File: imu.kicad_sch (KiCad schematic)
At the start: 4 parts, among them U8 MC3479

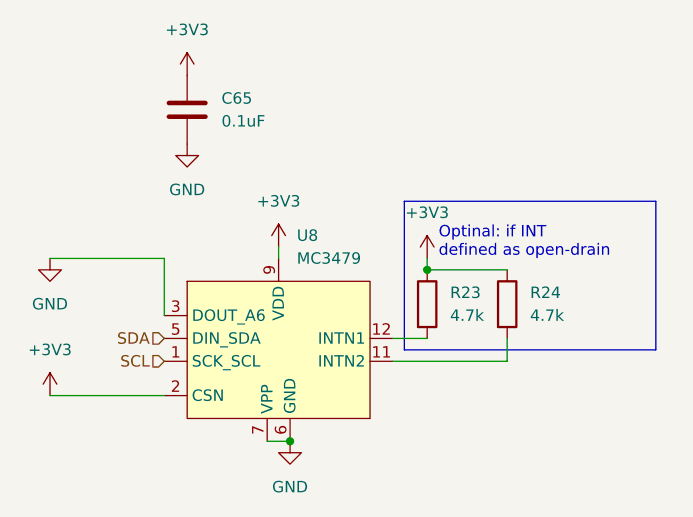
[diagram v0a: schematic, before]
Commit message: done first iteration of pcb routing, slikscreen still broken
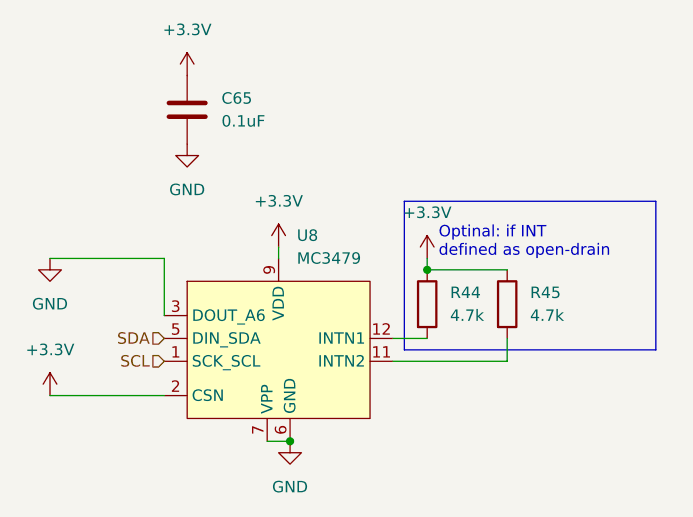
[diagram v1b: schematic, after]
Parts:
- renumbered R23 to R44, R24 to R45
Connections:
- net +3V3 renamed +3.3V
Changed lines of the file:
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@@
     (pin "2")
   )
-  (symbol (lib_id "power:+3V3") (at 140.97 86.36 0) (unit 1)
+  (symbol (lib_id "power:+3.3V") (at 140.97 86.36 0) (unit 1)
     (in_bom yes) (on_board yes) (fields_autoplaced)
-    (property "Reference" "#PWR075" (id 0) (at 140.97 90.17 0)
+    (property "Reference" "#PWR0235" (id 0) (at 140.97 90.17 0)
       (effects (font (size 1.27 1.27)) hide)
     )
-    (property "Value" "+3V3" (id 1) (at 140.97 81.28 0))
+    (property "Value" "+3.3V" (id 1) (at 140.97 81.28 0))
     (property "Footprint" "" (id 2) (at 140.97 86.36 0)
       (effects (font (size 1.27 1.27)) hide)
@@
   (symbol (lib_id "Device:R") (at 157.48 92.71 0) (unit 1)
     (in_bom yes) (on_board yes) (fields_autoplaced)
-    (property "Reference" "R23" (id 0) (at 160.02 91.4399 0)
+    (property "Reference" "R44" (id 0) (at 160.02 91.4399 0)
       (effects (font (size 1.27 1.27)) (justify left))
     )
@@
     (pin "2")
   )
-  (symbol (lib_id "power:+3V3") (at 130.81 67.31 0) (unit 1)
+  (symbol (lib_id "power:+3.3V") (at 130.81 67.31 0) (unit 1)
     (in_bom yes) (on_board yes) (fields_autoplaced)
-    (property "Reference" "#PWR073" (id 0) (at 130.81 71.12 0)
+    (property "Reference" "#PWR0234" (id 0) (at 130.81 71.12 0)
       (effects (font (size 1.27 1.27)) hide)
     )
-    (property "Value" "+3V3" (id 1) (at 130.81 62.23 0))
+    (property "Value" "+3.3V" (id 1) (at 130.81 62.23 0))
     (property "Footprint" "" (id 2) (at 130.81 67.31 0)
       (effects (font (size 1.27 1.27)) hide)
@@
     (pin "1")
   )
-  (symbol (lib_id "power:+3V3") (at 115.57 102.87 0) (unit 1)
-    (in_bom yes) (on_board yes) (fields_autoplaced)
-    (property "Reference" "#PWR072" (id 0) (at 115.57 106.68 0)
-      (effects (font (size 1.27 1.27)) hide)
-    )
-    (property "Value" "+3V3" (id 1) (at 115.57 97.79 0))
-    (property "Footprint" "" (id 2) (at 115.57 102.87 0)
-      (effects (font (size 1.27 1.27)) hide)
-    )
-    (property "Datasheet" "" (id 3) (at 115.57 102.87 0)
-      (effects (font (size 1.27 1.27)) hide)
-    )
-    (pin "1")
-  )
   (symbol (lib_id "power:GND") (at 115.57 87.63 0) (unit 1)
     (in_bom yes) (on_board yes) (fields_autoplaced)
-    (property "Reference" "#PWR071" (id 0) (at 115.57 93.98 0)
+    (property "Reference" "#PWR074" (id 0) (at 115.57 93.98 0)
       (effects (font (size 1.27 1.27)) hide)
     )
@@
   (symbol (lib_id "Device:R") (at 166.37 92.71 0) (unit 1)
     (in_bom yes) (on_board yes) (fields_autoplaced)
-    (property "Reference" "R24" (id 0) (at 168.91 91.4399 0)
+    (property "Reference" "R45" (id 0) (at 168.91 91.4399 0)
       (effects (font (size 1.27 1.27)) (justify left))
     )
@@
     (pin "2")
   )
-  (symbol (lib_id "power:+3V3") (at 157.48 87.63 0) (unit 1)
+  (symbol (lib_id "power:+3.3V") (at 157.48 87.63 0) (unit 1)
     (in_bom yes) (on_board yes) (fields_autoplaced)
-    (property "Reference" "#PWR077" (id 0) (at 157.48 91.44 0)
+    (property "Reference" "#PWR0233" (id 0) (at 157.48 91.44 0)
       (effects (font (size 1.27 1.27)) hide)
     )
-    (property "Value" "+3V3" (id 1) (at 157.48 82.55 0))
+    (property "Value" "+3.3V" (id 1) (at 157.48 82.55 0))
     (property "Footprint" "" (id 2) (at 157.48 87.63 0)
       (effects (font (size 1.27 1.27)) hide)
@@
   (symbol (lib_id "power:GND") (at 142.24 107.95 0) (unit 1)
     (in_bom yes) (on_board yes) (fields_autoplaced)
-    (property "Reference" "#PWR076" (id 0) (at 142.24 114.3 0)
+    (property "Reference" "#PWR079" (id 0) (at 142.24 114.3 0)
       (effects (font (size 1.27 1.27)) hide)
     )
@@
     (pin "1")
   )
+  (symbol (lib_id "power:+3.3V") (at 115.57 102.87 0) (unit 1)
+    (in_bom yes) (on_board yes) (fields_autoplaced)
+    (property "Reference" "#PWR0236" (id 0) (at 115.57 106.68 0)
+      (effects (font (size 1.27 1.27)) hide)
+    )
+    (property "Value" "+3.3V" (id 1) (at 115.57 97.79 0))
+    (property "Footprint" "" (id 2) (at 115.57 102.87 0)
+      (effects (font (size 1.27 1.27)) hide)
+    )
+    (property "Datasheet" "" (id 3) (at 115.57 102.87 0)
+      (effects (font (size 1.27 1.27)) hide)
+    )
+    (pin "1")
+  )
   (symbol (lib_id "power:GND") (at 130.81 74.93 0) (unit 1)
     (in_bom yes) (on_board yes) (fields_autoplaced)
-    (property "Reference" "#PWR074" (id 0) (at 130.81 81.28 0)
+    (property "Reference" "#PWR077" (id 0) (at 130.81 81.28 0)
       (effects (font (size 1.27 1.27)) hide)
     )

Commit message: mounting holes, fixes silkscreen
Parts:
- renumbered R44 to R43, R45 to R44
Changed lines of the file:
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@@
   (symbol (lib_id "power:+3.3V") (at 140.97 86.36 0) (unit 1)
     (in_bom yes) (on_board yes) (fields_autoplaced)
-    (property "Reference" "#PWR0235" (id 0) (at 140.97 90.17 0)
+    (property "Reference" "#PWR078" (id 0) (at 140.97 90.17 0)
       (effects (font (size 1.27 1.27)) hide)
     )
@@
   (symbol (lib_id "Device:R") (at 157.48 92.71 0) (unit 1)
     (in_bom yes) (on_board yes) (fields_autoplaced)
-    (property "Reference" "R44" (id 0) (at 160.02 91.4399 0)
+    (property "Reference" "R43" (id 0) (at 160.02 91.4399 0)
       (effects (font (size 1.27 1.27)) (justify left))
     )
@@
   (symbol (lib_id "power:+3.3V") (at 130.81 67.31 0) (unit 1)
     (in_bom yes) (on_board yes) (fields_autoplaced)
-    (property "Reference" "#PWR0234" (id 0) (at 130.81 71.12 0)
+    (property "Reference" "#PWR076" (id 0) (at 130.81 71.12 0)
       (effects (font (size 1.27 1.27)) hide)
     )
@@
   (symbol (lib_id "Device:R") (at 166.37 92.71 0) (unit 1)
     (in_bom yes) (on_board yes) (fields_autoplaced)
-    (property "Reference" "R45" (id 0) (at 168.91 91.4399 0)
+    (property "Reference" "R44" (id 0) (at 168.91 91.4399 0)
       (effects (font (size 1.27 1.27)) (justify left))
     )
@@
   (symbol (lib_id "power:+3.3V") (at 157.48 87.63 0) (unit 1)
     (in_bom yes) (on_board yes) (fields_autoplaced)
-    (property "Reference" "#PWR0233" (id 0) (at 157.48 91.44 0)
+    (property "Reference" "#PWR080" (id 0) (at 157.48 91.44 0)
       (effects (font (size 1.27 1.27)) hide)
     )
@@
   (symbol (lib_id "power:+3.3V") (at 115.57 102.87 0) (unit 1)
     (in_bom yes) (on_board yes) (fields_autoplaced)
-    (property "Reference" "#PWR0236" (id 0) (at 115.57 106.68 0)
+    (property "Reference" "#PWR075" (id 0) (at 115.57 106.68 0)
       (effects (font (size 1.27 1.27)) hide)
     )
